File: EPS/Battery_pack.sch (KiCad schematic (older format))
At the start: 11 parts

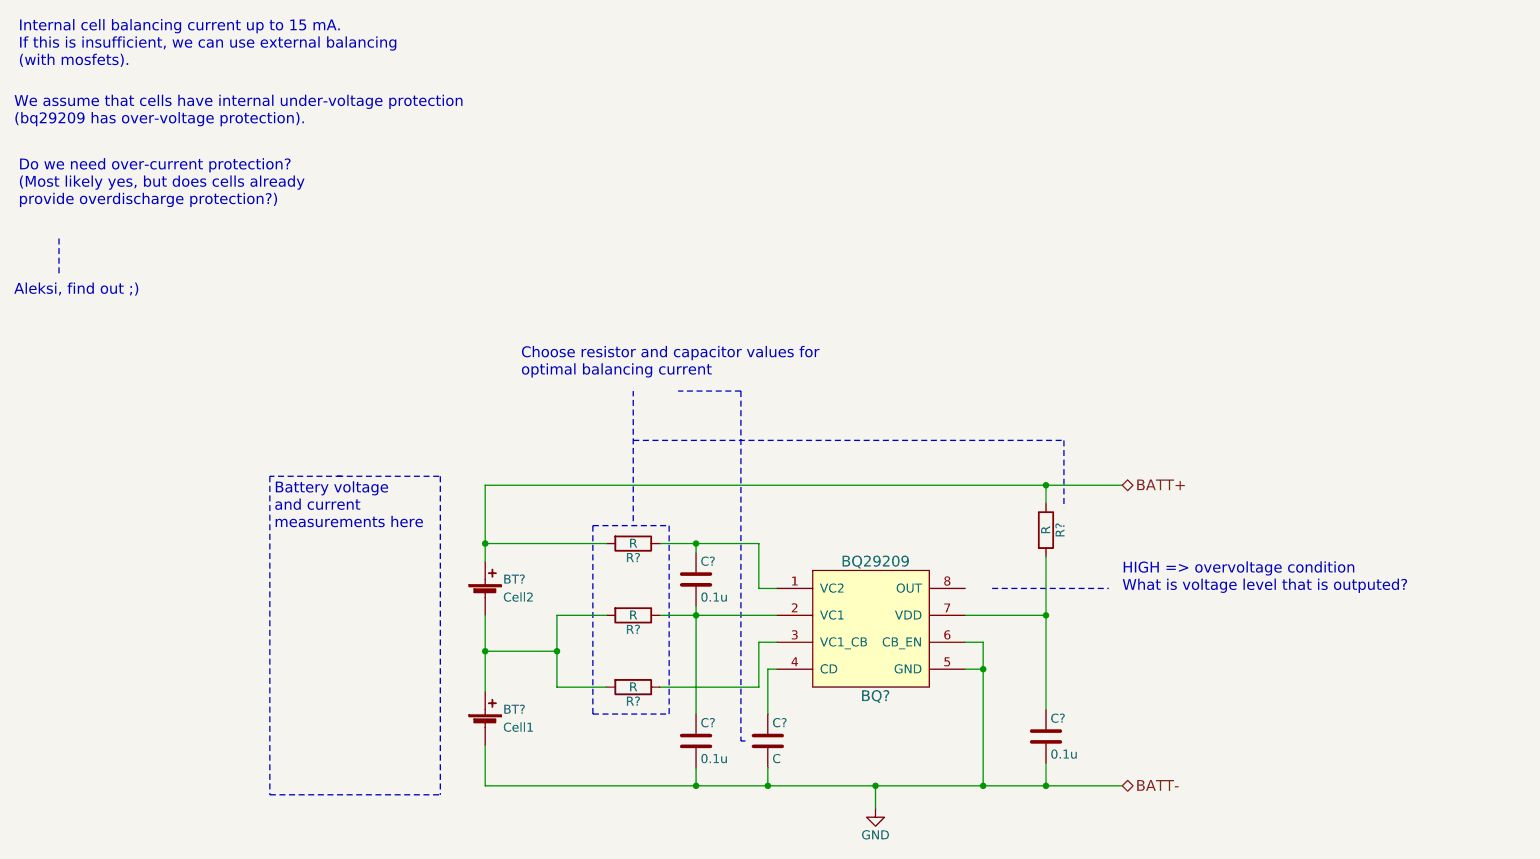
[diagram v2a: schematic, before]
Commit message: Finalized SCH (beta version) and started pcb
Capacitor banks might need to be reassigned to other locations.
No RBF pin on this SCH or PCB.
Battery gound deployment switch is fully mechanical (no mosfet switch on low side).
PCB of the prototype started. Main power converters and current measuring devices layed out.
SCH still requires ESD protection diodes!
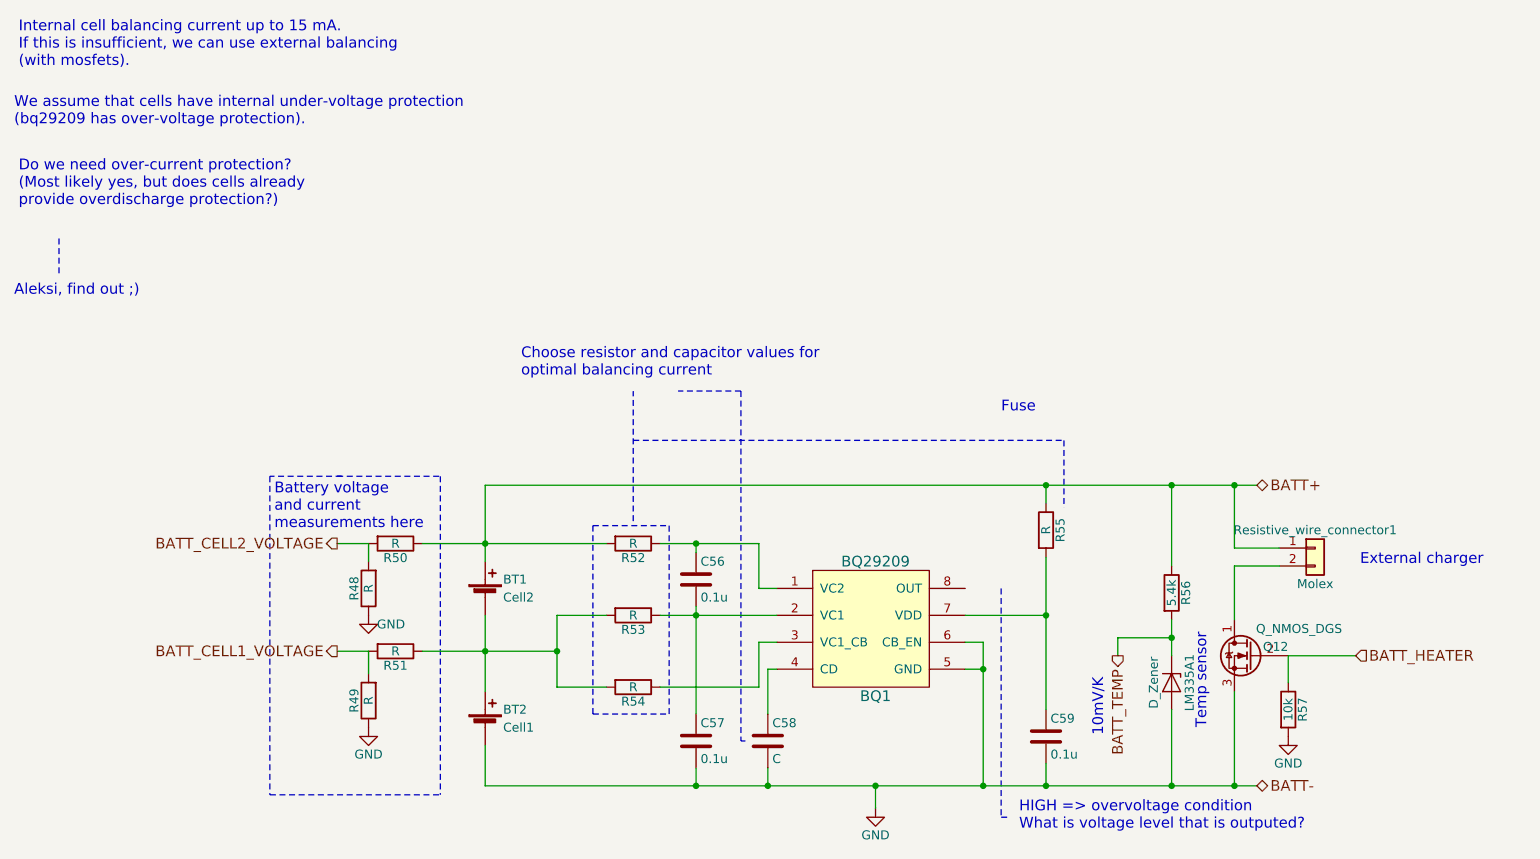
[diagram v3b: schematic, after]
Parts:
- added LM335A1: D_Zener, TO_SOT_Packages_THT:TO-92_Inline_Narrow_Oval, symbol D_Zener
- added Q12: Q_NMOS_DGS, TO_SOT_Packages_SMD:SOT-23, symbol Q_NMOS_DGS
- added R48, R49, R50, R51: R, Resistors_SMD:R_0603, symbol R
- added R56: 5.4k, Resistors_SMD:R_0603, symbol R
- added R57: 10k, Resistors_SMD:R_0603, symbol R
- added Resistive_wire_connector1: Molex, Connectors_Molex:Molex_KK-6410-02_02x2.54mm_Straight, symbol Conn_01x02
- BQ1: renamed from BQ?; footprint (none) -> Housings_SON:Texas_S-PVSON-N8
- BT1, BT2: renamed from BT?; footprint (none) -> Battery_Holder_Lib:18650_Holder_FULL
- C56, C57, C58, C59: renamed from C?; footprint (none) -> Capacitors_SMD:C_0603
- R52, R53, R54, R55: renamed from R?; footprint (none) -> Resistors_SMD:R_0603
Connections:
- net BATT+: now also R50.1, R56.1, Resistive_wire_connector1.1 (Pin_1)
- net GND: now also LM335A1.2 (A), Q12.3 (S), R48.1, R49.1, R57.2
- net at BT1.2 (-), BT2.1 (+), R53.2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: now also R51.1
- new net: Q12.1 (D), Resistive_wire_connector1.2 (Pin_2)
- new net BATT_CELL1_VOLTAGE: R49.2, R51.2
- new net BATT_CELL2_VOLTAGE: R48.2, R50.2
- new net BATT_HEATER: Q12.2 (G), R57.1
- new net BATT_TEMP: LM335A1.1 (K), R56.2
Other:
- note added: "10mV/K"
- note added: "External charger"
- note added: "Fuse"
- note added: "Temp sensor"

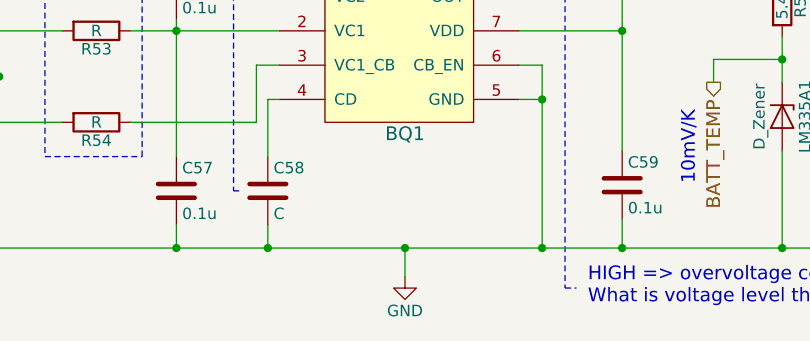
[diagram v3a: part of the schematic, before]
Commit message: Fixed gnd at Battery_pack.sch
No global gnd at BP.sch
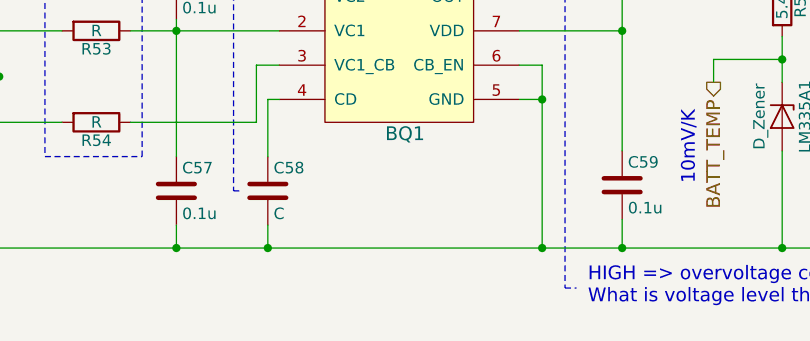
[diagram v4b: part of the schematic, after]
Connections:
- net GND: no longer BQ1.5 (GND), BQ1.6 (CB_EN), BT2.2 (-), C57.2, C58.2, C59.2, LM335A1.2 (A), Q12.3 (S)
- new net BATT-: BQ1.5 (GND), BQ1.6 (CB_EN), BT2.2 (-), C57.2, C58.2, C59.2, LM335A1.2 (A), Q12.3 (S)
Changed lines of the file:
@@
 Text HLabel 7825 3450 2    60   BiDi ~ 0
 BATT+
-$Comp
-L GND #PWR0153
-U 1 1 5A87BAD8
-P 5700 5250
-F 0 "#PWR0153" H 5700 5000 50  0001 C CNN
-F 1 "GND" H 5700 5100 50  0000 C CNN
-F 2 "" H 5700 5250 50  0001 C CNN
-F 3 "" H 5700 5250 50  0001 C CNN
-	1    5700 5250
-	1    0    0    -1
-$EndComp
 Text Notes 6500 5375 0    60   ~ 0
 HIGH => overvoltage condition\nWhat is voltage level that is outputed?
@@
 Connection ~ 6300 5125
 Connection ~ 6650 5125
-Wire Wire Line
-	5700 5250 5700 5125
-Connection ~ 5700 5125
 Wire Notes Line
 	4350 3650 4350 2925

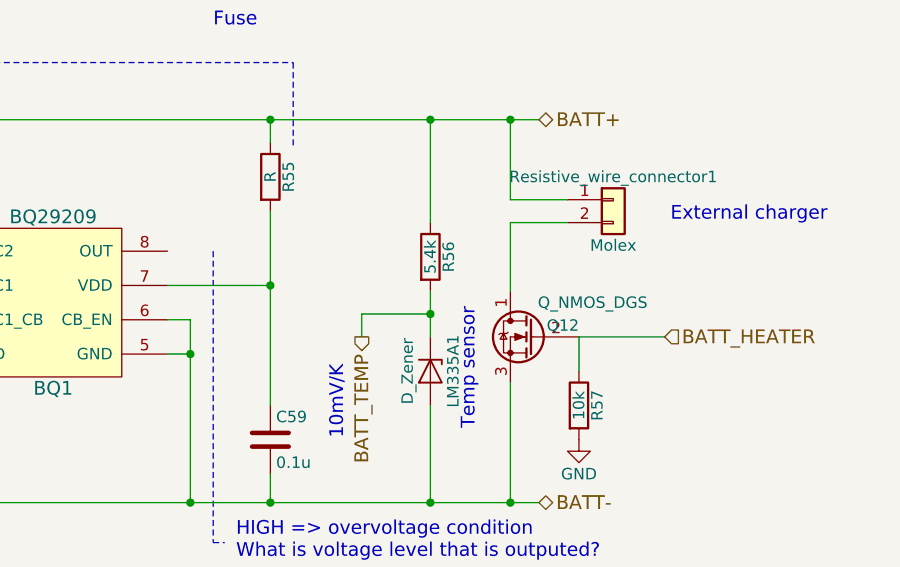
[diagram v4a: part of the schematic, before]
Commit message: PCB updated
Added testpoints and updated PCB
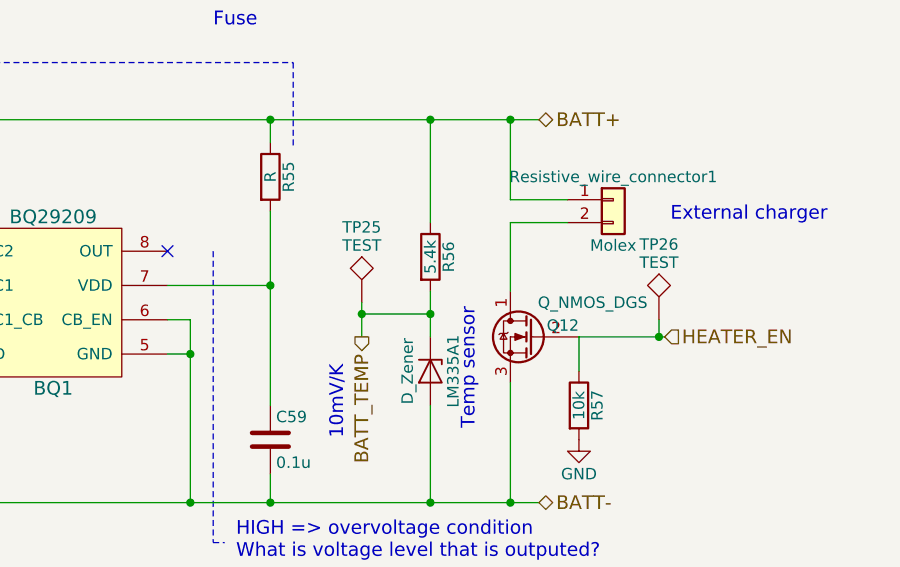
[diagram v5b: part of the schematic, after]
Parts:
- added TP25, TP26: TEST, Measurement_Points:Measurement_Point_Round-SMD-Pad_Small, symbol TEST
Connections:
- net BATT_TEMP: now also TP25.1
- net BATT_HEATER renamed HEATER_EN
- net HEATER_EN: now also TP26.1
- no-connect marks 0 -> 1
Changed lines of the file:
@@
 $EndComp
 $Comp
-L GND #PWR0154
+L GND #PWR0151
 U 1 1 5A8DAE81
 P 8000 4850
-F 0 "#PWR0154" H 8000 4600 50  0001 C CNN
+F 0 "#PWR0151" H 8000 4600 50  0001 C CNN
 F 1 "GND" H 8000 4700 50  0000 C CNN
 F 2 "" H 8000 4850 50  0001 C CNN
@@
 $EndComp
 Text HLabel 8375 4400 2    60   Input ~ 0
-BATT_HEATER
+HEATER_EN
 $Comp
 L R R50
@@
 $EndComp
 $Comp
-L GND #PWR0155
+L GND #PWR0152
 U 1 1 5A8ECDA3
 P 2875 4175
-F 0 "#PWR0155" H 2875 3925 50  0001 C CNN
+F 0 "#PWR0152" H 2875 3925 50  0001 C CNN
 F 1 "GND" H 3000 4125 50  0000 C CNN
 F 2 "" H 2875 4175 50  0001 C CNN
@@
 $EndComp
 $Comp
-L GND #PWR0156
+L GND #PWR0153
 U 1 1 5A8ECDEB
 P 2875 4800
-F 0 "#PWR0156" H 2875 4550 50  0001 C CNN
+F 0 "#PWR0153" H 2875 4550 50  0001 C CNN
 F 1 "GND" H 2875 4650 50  0000 C CNN
 F 2 "" H 2875 4800 50  0001 C CNN
@@
 Wire Wire Line
 	3175 4375 3925 4375
-Wire Wire Line
-	3525 4175 3525 4600
 Connection ~ 3925 4375
-Connection ~ 3525 4375
 Connection ~ 4700 4175
 Wire Wire Line
@@
 	7350 4300 7050 4300
 Wire Wire Line
-	7050 4300 7050 4400
+	7050 4250 7050 4400
 Connection ~ 7350 3450
 Wire Wire Line
@@
 Text Notes 6975 4850 1    60   ~ 0
 10mV/K
+NoConn ~ 6200 4025
+$Comp
+L TEST TP26
+U 1 1 5A9EFC6C
+P 8350 4325
+F 0 "TP26" H 8350 4625 50  0000 C BNN
+F 1 "TEST" H 8350 4575 50  0000 C CNN
+F 2 "Measurement_Points:Measurement_Point_Round-SMD-Pad_Small" H 8350 4325 50  0001 C CNN
+F 3 "" H 8350 4325 50  0001 C CNN
+	1    8350 4325
+	1    0    0    -1
+$EndComp
+Wire Wire Line
+	8350 4325 8350 4400
+Connection ~ 8350 4400
+$Comp
+L TEST TP25
+U 1 1 5A9EFE34
+P 7050 4250
+F 0 "TP25" H 7050 4550 50  0000 C BNN
+F 1 "TEST" H 7050 4500 50  0000 C CNN
+F 2 "Measurement_Points:Measurement_Point_Round-SMD-Pad_Small" H 7050 4250 50  0001 C CNN
+F 3 "" H 7050 4250 50  0001 C CNN
+	1    7050 4250
+	1    0    0    -1
+$EndComp
+Connection ~ 7050 4300
+Wire Wire Line
+	3525 4175 3525 4600
+Connection ~ 3525 4375
 $EndSCHEMATC

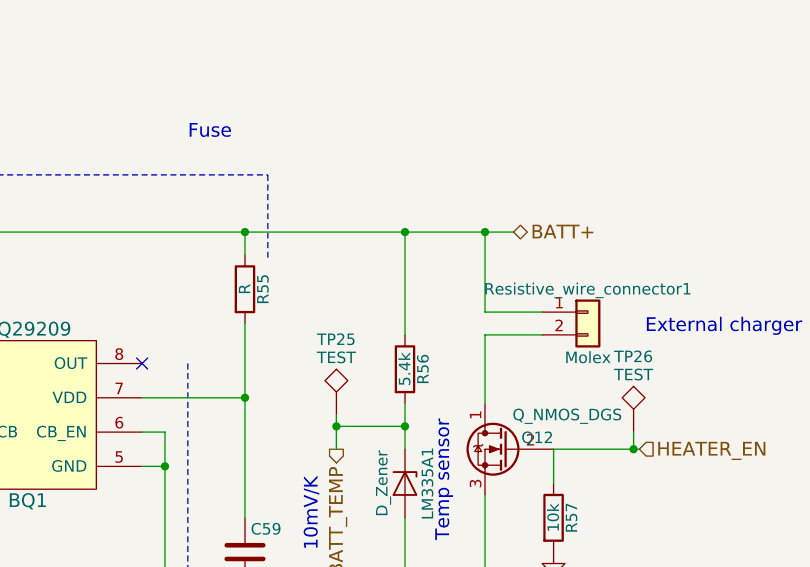
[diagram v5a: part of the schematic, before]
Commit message: Updated PCB
PCB requires mcu to be routed.
Changed to thermistor connector on pcb
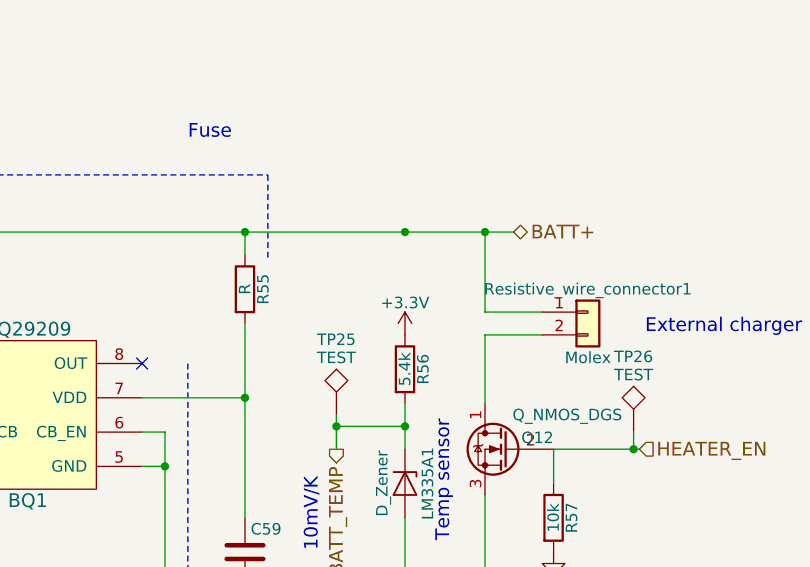
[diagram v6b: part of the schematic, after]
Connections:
- net BATT+: no longer R56.1
- new net +3V3: R56.1
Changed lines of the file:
@@
 Wire Wire Line
 	7350 4200 7350 4400
-Wire Wire Line
-	7350 3450 7350 3900
 Connection ~ 7350 4300
 Wire Wire Line
@@
 	3525 4175 3525 4600
 Connection ~ 3525 4375
+$Comp
+L +3.3V #PWR?
+U 1 1 5AA008D8
+P 7350 3900
+F 0 "#PWR?" H 7350 3750 50  0001 C CNN
+F 1 "+3.3V" H 7350 4040 50  0000 C CNN
+F 2 "" H 7350 3900 50  0001 C CNN
+F 3 "" H 7350 3900 50  0001 C CNN
+	1    7350 3900
+	1    0    0    -1
+$EndComp
 $EndSCHEMATC
